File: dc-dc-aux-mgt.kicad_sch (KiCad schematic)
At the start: 42 parts, among them U19 MPM54304GMN, U25 PAC1720-1, U3 PAC1720-1

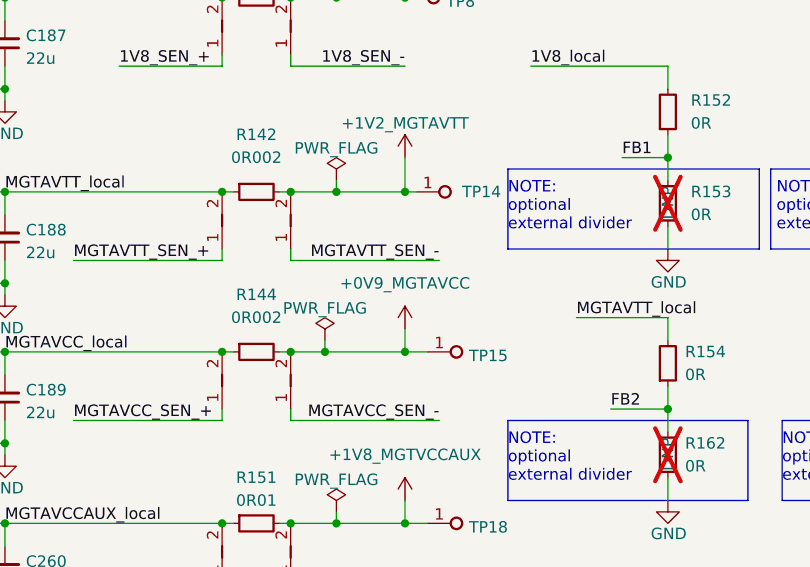
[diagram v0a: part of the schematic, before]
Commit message: [#68543] Migrate to KiCad 8
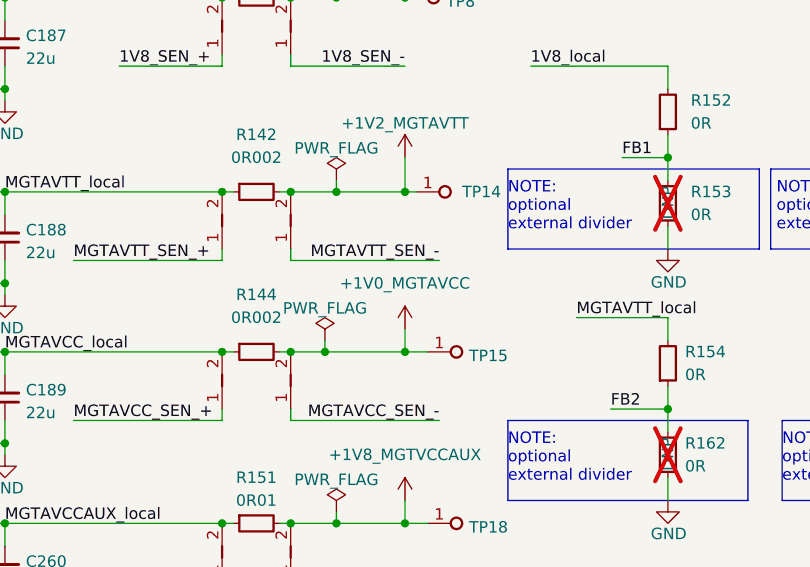
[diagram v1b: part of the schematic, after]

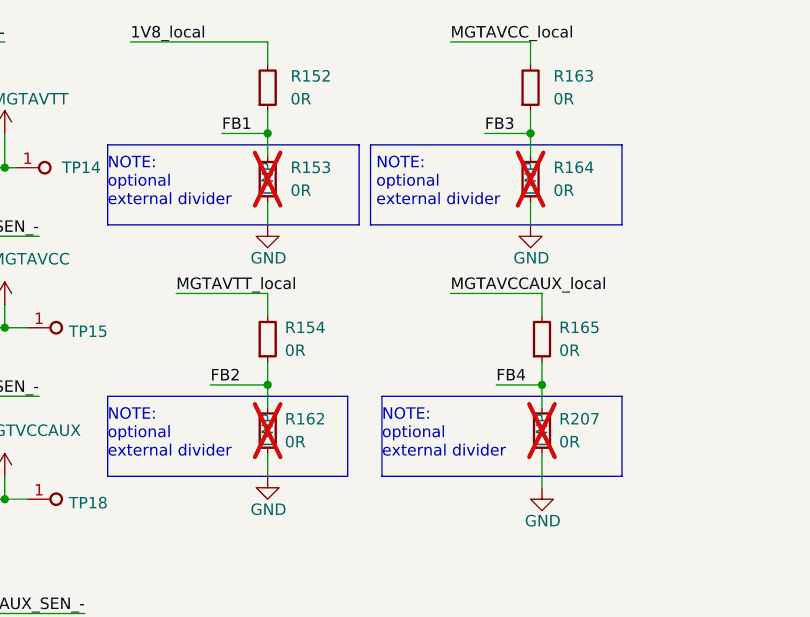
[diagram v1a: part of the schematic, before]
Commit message: [#69629] Fix DNP attributes
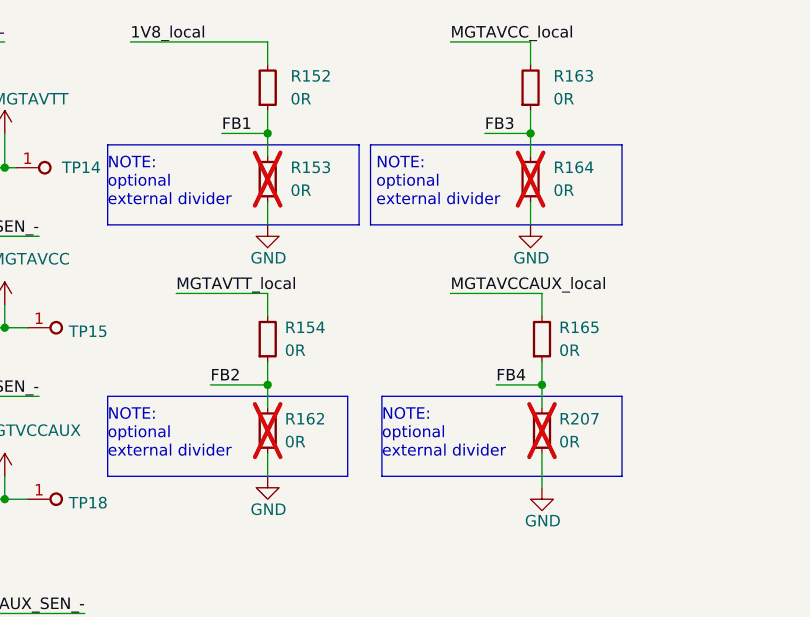
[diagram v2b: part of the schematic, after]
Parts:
- R153, R162, R164, R207: DNP DNP -> (none)

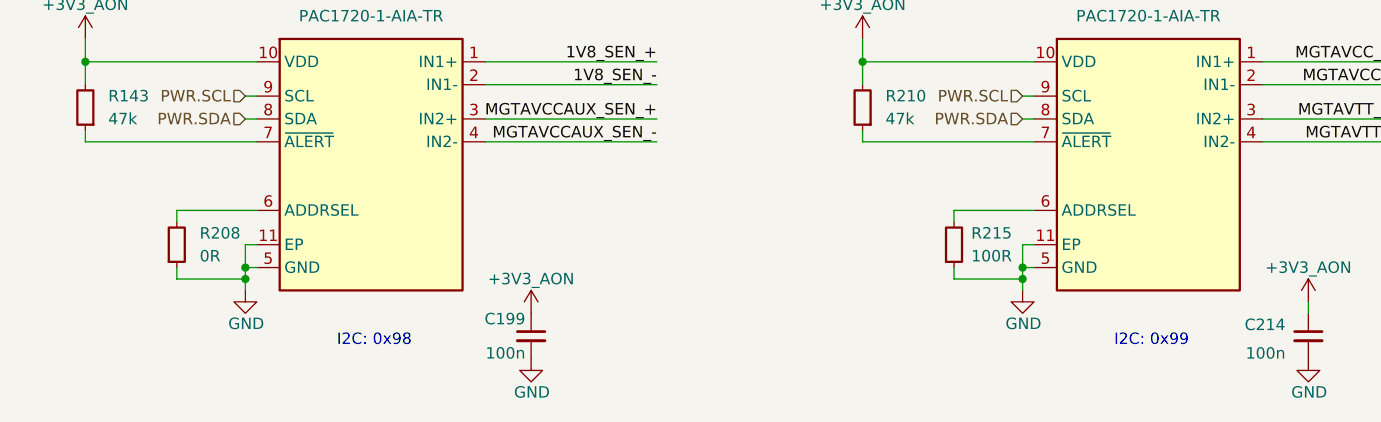
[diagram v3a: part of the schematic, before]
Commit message: [#69798] Fix I2C adresses descriptions on the schematic
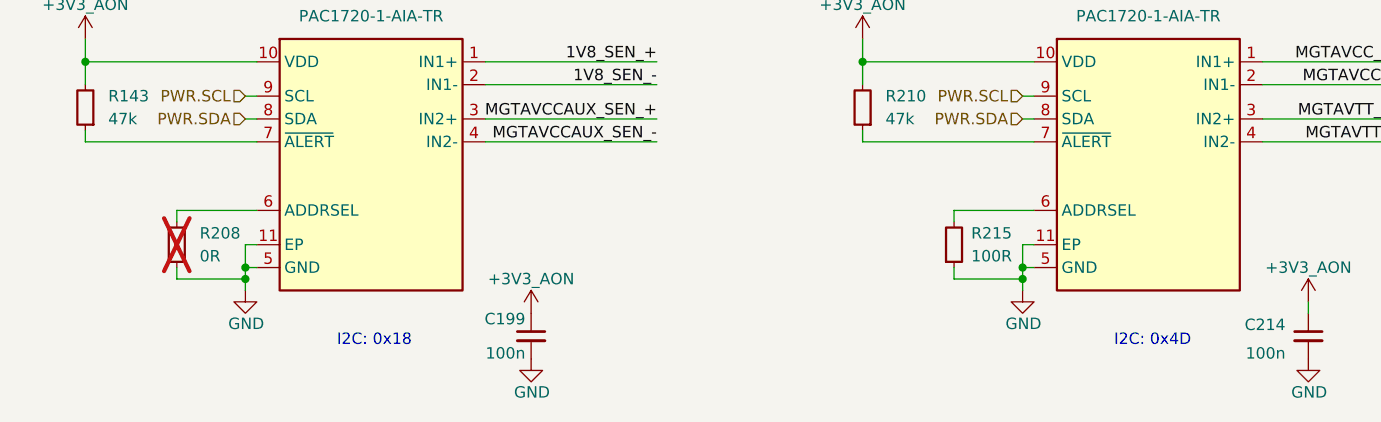
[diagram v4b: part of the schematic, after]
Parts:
- R208: now not fitted; now left out of the parts list
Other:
- note added: "I2C: 0x18"
- note added: "I2C: 0x4D"
- note removed: "I2C: 0x98"
- note removed: "I2C: 0x99"
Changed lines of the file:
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@@
 		)
 	)
-	(text "I2C: 0x99"
+	(text "I2C: 0x4D"
 		(exclude_from_sim no)
 		(at 250.19 224.79 0)
@@
 		)
 	)
-	(text "I2C: 0x98"
+	(text "I2C: 0x18"
 		(exclude_from_sim no)
 		(at 163.83 224.79 0)
@@
 		(unit 1)
 		(exclude_from_sim no)
-		(in_bom yes)
+		(in_bom no)
 		(on_board yes)
-		(dnp no)
+		(dnp yes)
 		(fields_autoplaced yes)
 		(property "Reference" "R208"

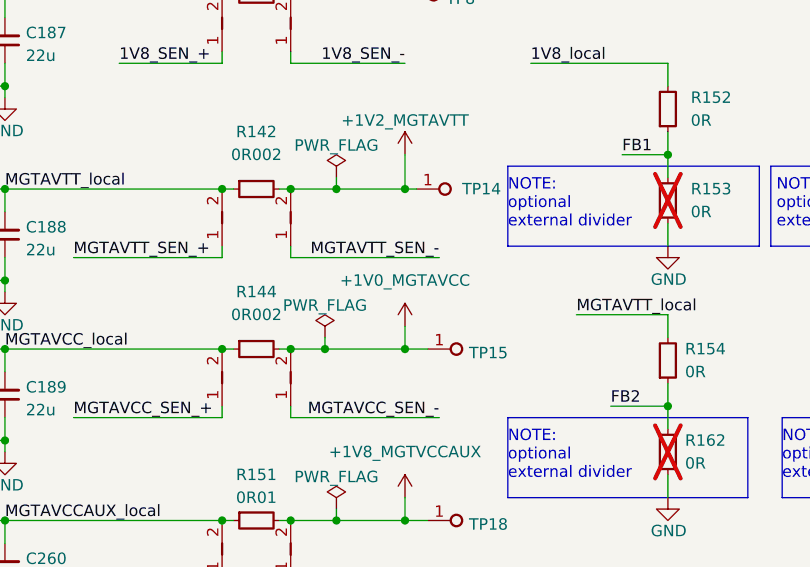
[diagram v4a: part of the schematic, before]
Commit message: [#70235] Improve power supply labels
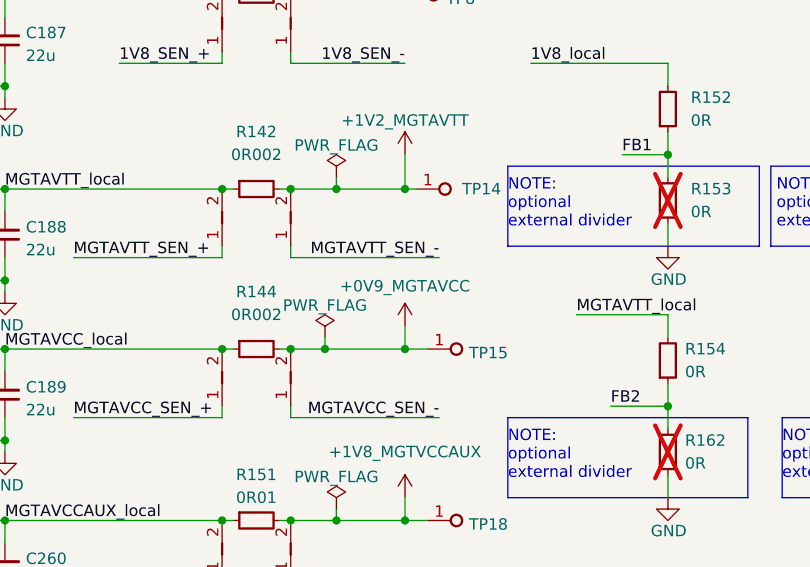
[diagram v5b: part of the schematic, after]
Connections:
- net +1V0_MGTAVCC renamed +0V9_MGTAVCC
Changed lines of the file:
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@@
 	)
 	(symbol
+		(lib_id "antmicropower:+0V9_MGTAVCC")
+		(at 229.87 90.17 0)
+		(unit 1)
+		(exclude_from_sim no)
+		(in_bom yes)
+		(on_board yes)
+		(dnp no)
+		(property "Reference" "#PWR058"
+			(at 229.87 93.98 0)
+			(effects
+				(font
+					(size 1.27 1.27)
+				)
+				(hide yes)
+			)
+		)
+		(property "Value" "+0V9_MGTAVCC"
+			(at 229.87 85.725 0)
+			(effects
+				(font
+					(size 1.27 1.27)
+				)
+			)
+		)
+		(property "Footprint" ""
+			(at 229.87 90.17 0)
+			(effects
+				(font
+					(size 1.27 1.27)
+				)
+				(hide yes)
+			)
+		)
+		(property "Datasheet" ""
+			(at 229.87 90.17 0)
+			(effects
+				(font
+					(size 1.27 1.27)
+				)
+				(hide yes)
+			)
+		)
+		(property "Description" ""
+			(at 229.87 90.17 0)
+			(effects
+				(font
+					(size 1.27 1.27)
+				)
+				(hide yes)
+			)
+		)
+		(pin "1"
+		)
+		(instances
+			(project "data-center-rdimm-ddr5-tester"
+				(path "/1faa6543-e26a-4449-8bac-ee14b9f19e5f/00000000-0000-0000-0000-000060225b0c/0d757288-805e-4f45-ad8e-e9ee6afc6379"
+					(reference "#PWR058")
+					(unit 1)
+				)
+			)
+		)
+	)
+	(symbol
 		(lib_id "antmicropower:GND")
 		(at 185.42 86.36 0)
@@
 					(unit 1)
 				)
-			)
-		)
-	)
-	(symbol
-		(lib_id "antmicropower:+0V9_MGTAVCC")
-		(at 229.87 90.17 0)
-		(unit 1)
-		(exclude_from_sim no)
-		(in_bom yes)
-		(on_board yes)
-		(dnp no)
-		(fields_autoplaced yes)
-		(property "Reference" "#PWR0335"
-			(at 229.87 93.98 0)
-			(effects
-				(font
-					(size 1.27 1.27)
-				)
-				(hide yes)
-			)
-		)
-		(property "Value" "+1V0_MGTAVCC"
-			(at 229.87 85.09 0)
-			(effects
-				(font
-					(size 1.27 1.27)
-				)
-			)
-		)
-		(property "Footprint" ""
-			(at 229.87 90.17 0)
-			(effects
-				(font
-					(size 1.27 1.27)
-				)
-				(hide yes)
-			)
-		)
-		(property "Datasheet" ""
-			(at 229.87 90.17 0)
-			(effects
-				(font
-					(size 1.27 1.27)
-				)
-				(hide yes)
-			)
-		)
-		(property "Description" ""
-			(at 229.87 90.17 0)
-			(effects
-				(font
-					(size 1.27 1.27)
-				)
-				(hide yes)
-			)
-		)
-		(pin "1"
-		)
-		(instances
-			(project "data-center-rdimm-ddr5-tester"
-				(path "/1faa6543-e26a-4449-8bac-ee14b9f19e5f/00000000-0000-0000-0000-000060225b0c/0d757288-805e-4f45-ad8e-e9ee6afc6379"
-					(reference "#PWR0335")
-					(unit 1)
-				)
